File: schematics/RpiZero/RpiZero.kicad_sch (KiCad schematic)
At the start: 1 part, among them U1 8_cells_battery

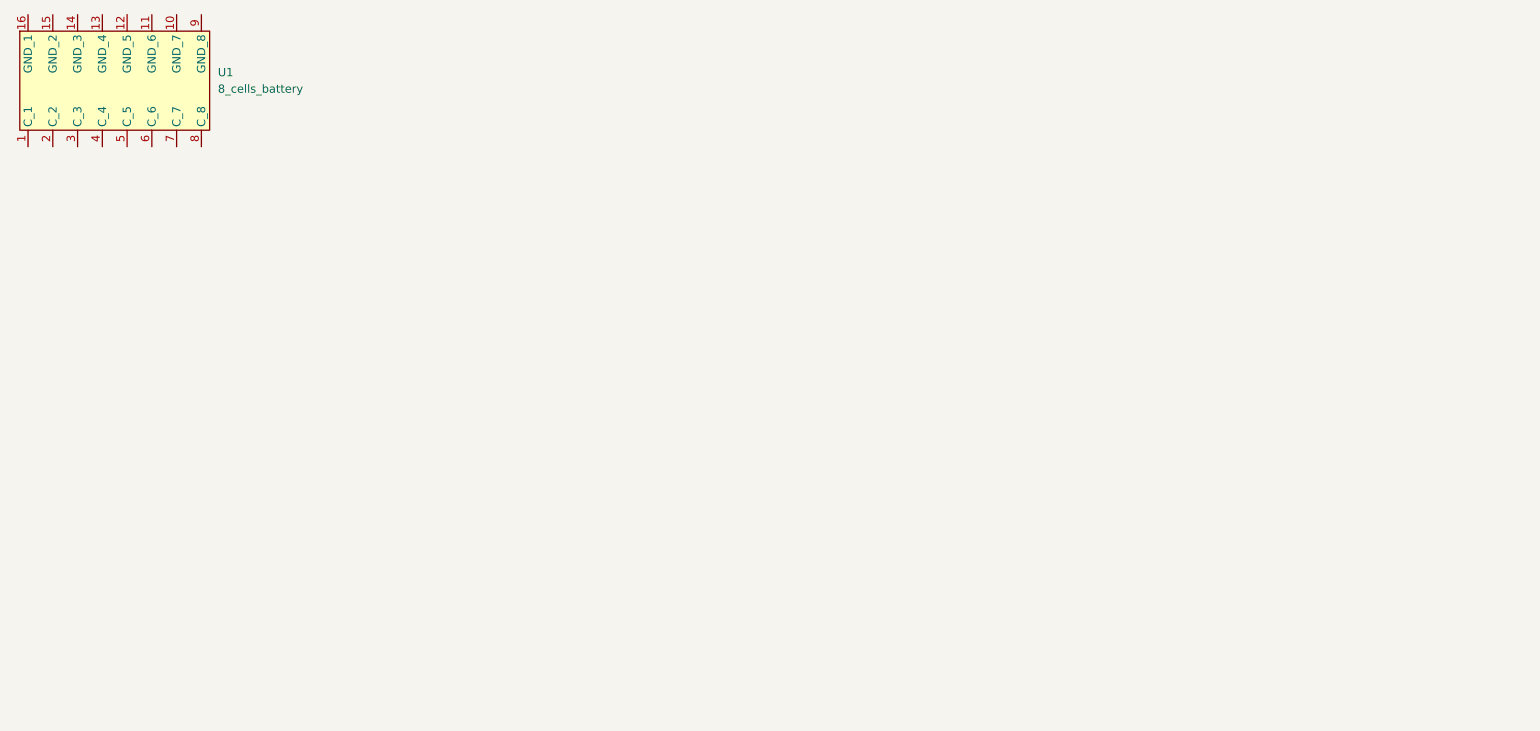
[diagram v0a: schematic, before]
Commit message: Update: added ADC MUX, voltage reference and battery pack symbol
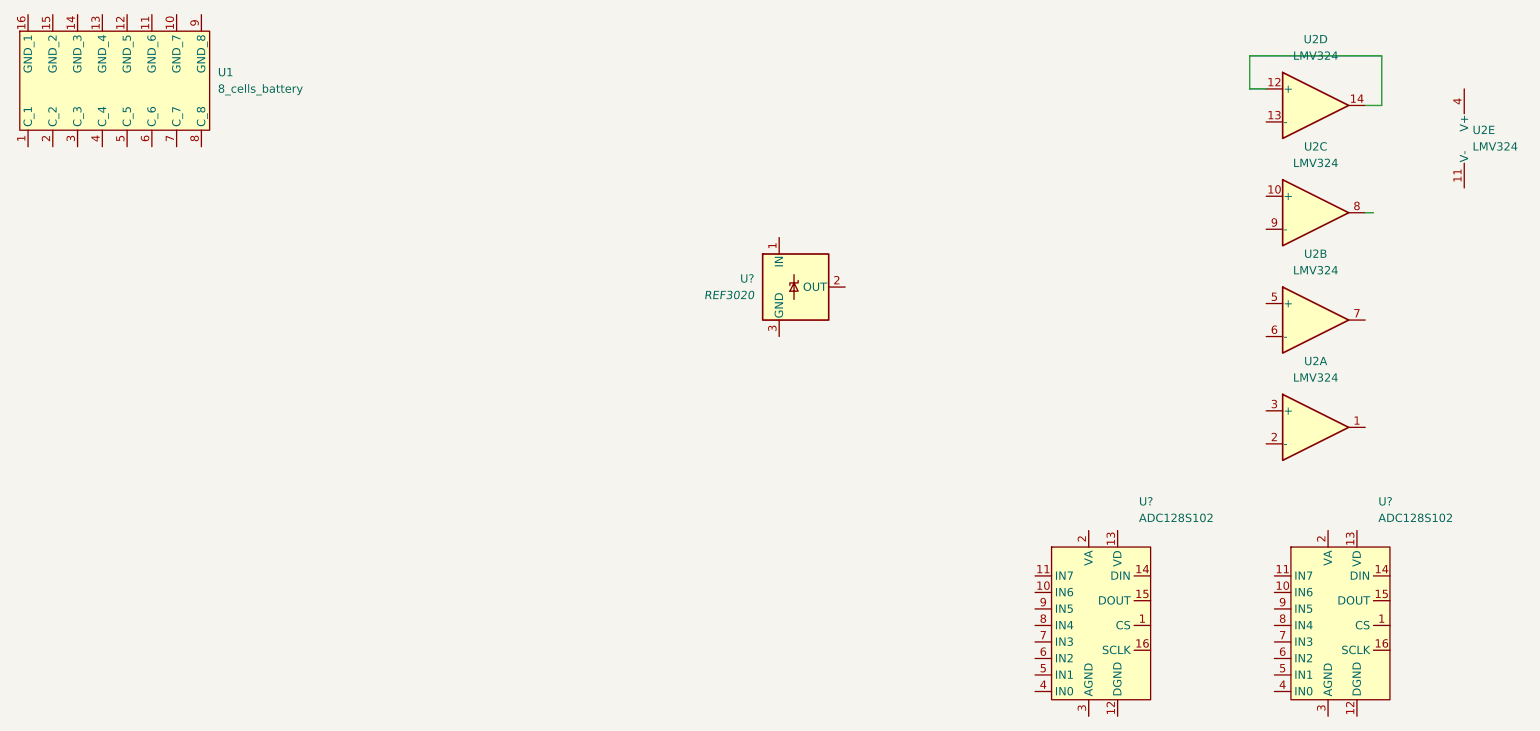
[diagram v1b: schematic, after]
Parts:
- added U2: LMV324, symbol Amplifier_Operational:LMV324
- added U? (x2): ADC128S102, Package_SO:TSSOP-16_4.4x5mm_P0.65mm, symbol Rpizero:ADC128S102
- added U?: REF3020, Package_TO_SOT_SMD:SOT-23, symbol Reference_Voltage:REF3020
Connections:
- new net: U2.12 (+), U2.14
